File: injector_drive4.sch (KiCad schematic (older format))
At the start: 17 parts, among them P32 CONN_1, P33 CONN_1, Q16 PIP-3104, Q17 HALL

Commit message: Removed LM1815 options. Now adaptive mode and square waves are the default,
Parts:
- C52: Field1 (none) -> newark,97M4148; Field2 (none) -> vendor1, smd w hem; Field3 (none) -> vendor2, thru w hem; Field4 (none) -> vendor2, smd w hem; Field5 (none) -> 200,V; Field6 (none) -> 10,%; Field7 (none) -> Multilayer Ceramic; Field8 (none) -> other,more,stuff
- D88, D91: Field1 (none) -> vendor1, thru w hem; Field2 (none) -> vendor1, smd w hem; Field3 (none) -> vendor2, thru w hem; Field4 (none) -> vendor2, smd w hem; Field5 (none) -> reverse,V; Field6 (none) -> current,A; Field7 (none) -> x; Field8 (none) -> other,more,stuff
- D89: Field1 (none) -> newark,18M3533; Field2 (none) -> vendor1, smd w hem; Field3 (none) -> vendor2, thru w hem; Field4 (none) -> vendor2, smd w hem; Field5 (none) -> 500,mW; Field6 (none) -> 20,mA; Field7 (none) -> X; Field8 (none) -> other,more,stuff
- D90: Field1 (none) -> newark,58K2469; Field2 (none) -> vendor1, smd w hem; Field3 (none) -> vendor2, thru w hem; Field4 (none) -> vendor2, smd w hem; Field5 (none) -> x,x; Field6 (none) -> x,x; Field7 (none) -> construct; Field8 (none) -> other,more,stuff
- L4: Field1 (none) -> vendor1, thru w hem; Field2 (none) -> vendor1, smd w hem; Field3 (none) -> vendor2, thru w hem; Field4 (none) -> vendor2, smd w hem; Field5 (none) -> x,x; Field6 (none) -> x,x; Field7 (none) -> x; Field8 (none) -> other,more,stuff
- Q16: Field1 (none) -> digi,PIP3104-ND; Field2 (none) -> vendor1, smd w hem; Field3 (none) -> vendor2, thru w hem; Field4 (none) -> vendor2, smd w hem; Field5 (none) -> 8,A; Field6 (none) -> x,x; Field7 (none) -> TOPFET; Field8 (none) -> other,more,stuff
- Q17: Field1 (none) -> digi,480-2002-ND; Field2 (none) -> vendor1, smd w hem; Field3 (none) -> vendor2, thru w hem; Field4 (none) -> vendor2, smd w hem; Field5 (none) -> x,x; Field6 (none) -> x,x; Field7 (none) -> x; Field8 (none) -> other,more,stuff
- R122: Field1 (none) -> newark,38k0327; Field2 (none) -> vendor1, smd w hem; Field3 (none) -> vendor2, thru w hem; Field4 (none) -> vendor2, smd w hem; Field5 (none) -> 250,mW; Field6 (none) -> 5,%; Field7 (none) -> carbon film; Field8 (none) -> other,more,stuff
- R123: Field1 (none) -> newark,38K0329; Field2 (none) -> vendor1, smd w hem; Field3 (none) -> vendor2, thru w hem; Field4 (none) -> vendor2, smd w hem; Field5 (none) -> 250,mW; Field6 (none) -> 5,%; Field7 (none) -> carbon film; Field8 (none) -> other,more,stuff
- R124: Field1 (none) -> newark,38k0352; Field2 (none) -> vendor1, smd w hem; Field3 (none) -> vendor2, thru w hem; Field4 (none) -> vendor2, smd w hem; Field5 (none) -> 250,mW; Field6 (none) -> 5,%; Field7 (none) -> carbon film; Field8 (none) -> other,more,stuff
- R125: Field1 (none) -> vendor1, thru w hem; Field2 (none) -> vendor1, smd w hem; Field3 (none) -> vendor2, thru w hem; Field4 (none) -> vendor2, smd w hem; Field5 (none) -> power,W; Field6 (none) -> tol,%; Field7 (none) -> construct; Field8 (none) -> other,more,stuff
- R126: Field1 (none) -> newark,38K0352; Field2 (none) -> vendor1, smd w hem; Field3 (none) -> vendor2, thru w hem; Field4 (none) -> vendor2, smd w hem; Field5 (none) -> 250,mW; Field6 (none) -> 5,%; Field7 (none) -> carbon film; Field8 (none) -> other,more,stuff
- R127: Field1 (none) -> newark,59K8561; Field2 (none) -> vendor1, smd w hem; Field3 (none) -> vendor2, thru w hem; Field4 (none) -> vendor2, smd w hem; Field5 (none) -> 1,W; Field6 (none) -> 5,%; Field7 (none) -> construct; Field8 (none) -> other,more,stuff
- R128: Field1 (none) -> newark,38K0340; Field2 (none) -> vendor1, smd w hem; Field3 (none) -> vendor2, thru w hem; Field4 (none) -> vendor2, smd w hem; Field5 (none) -> 1/4,W; Field6 (none) -> 5,%; Field7 (none) -> carbon film; Field8 (none) -> other,more,stuff

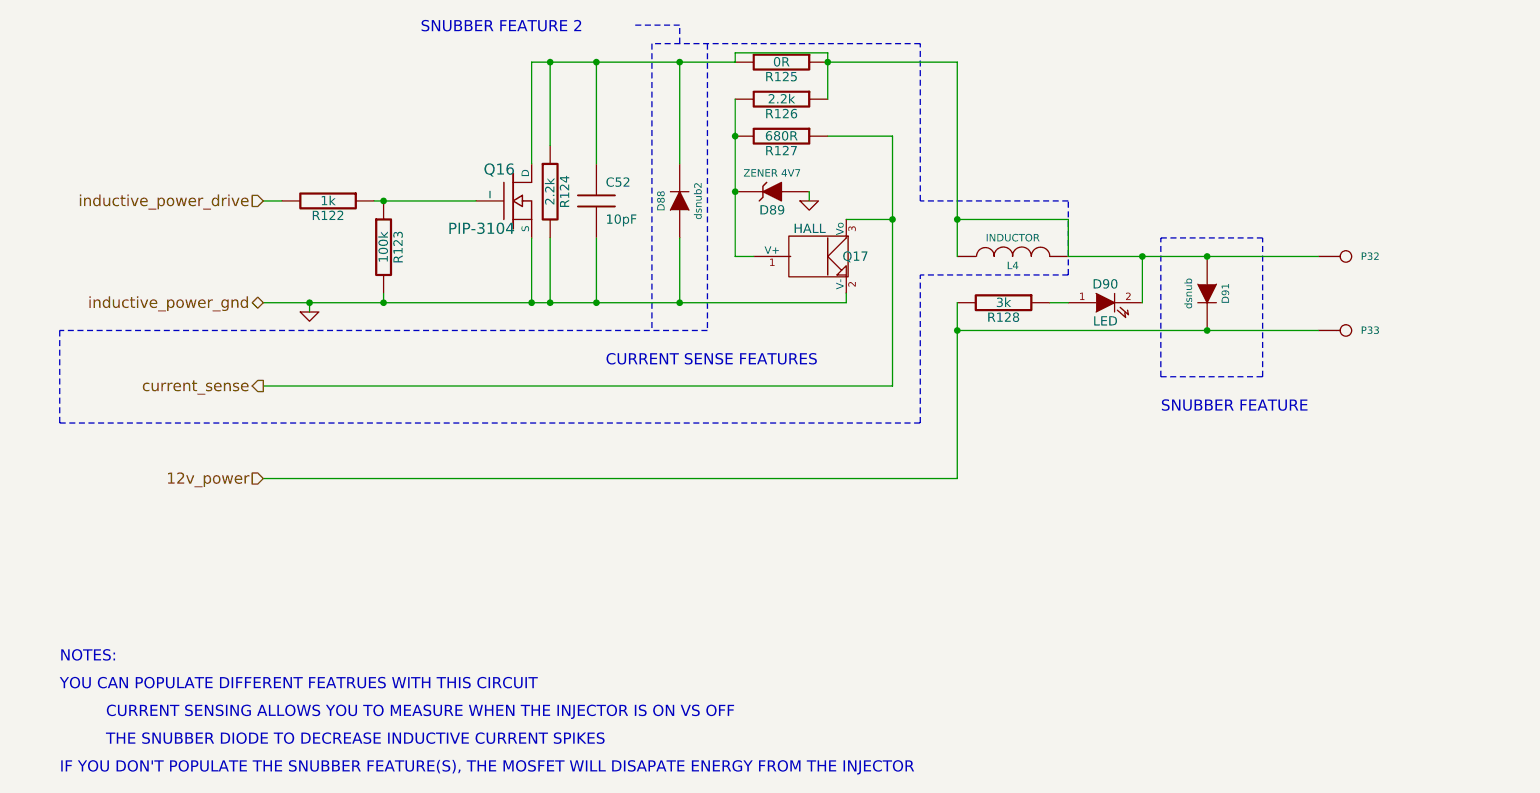
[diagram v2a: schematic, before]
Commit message: Implemented P&H, removed current sense circuitry, removed all unnecessary files from the repo
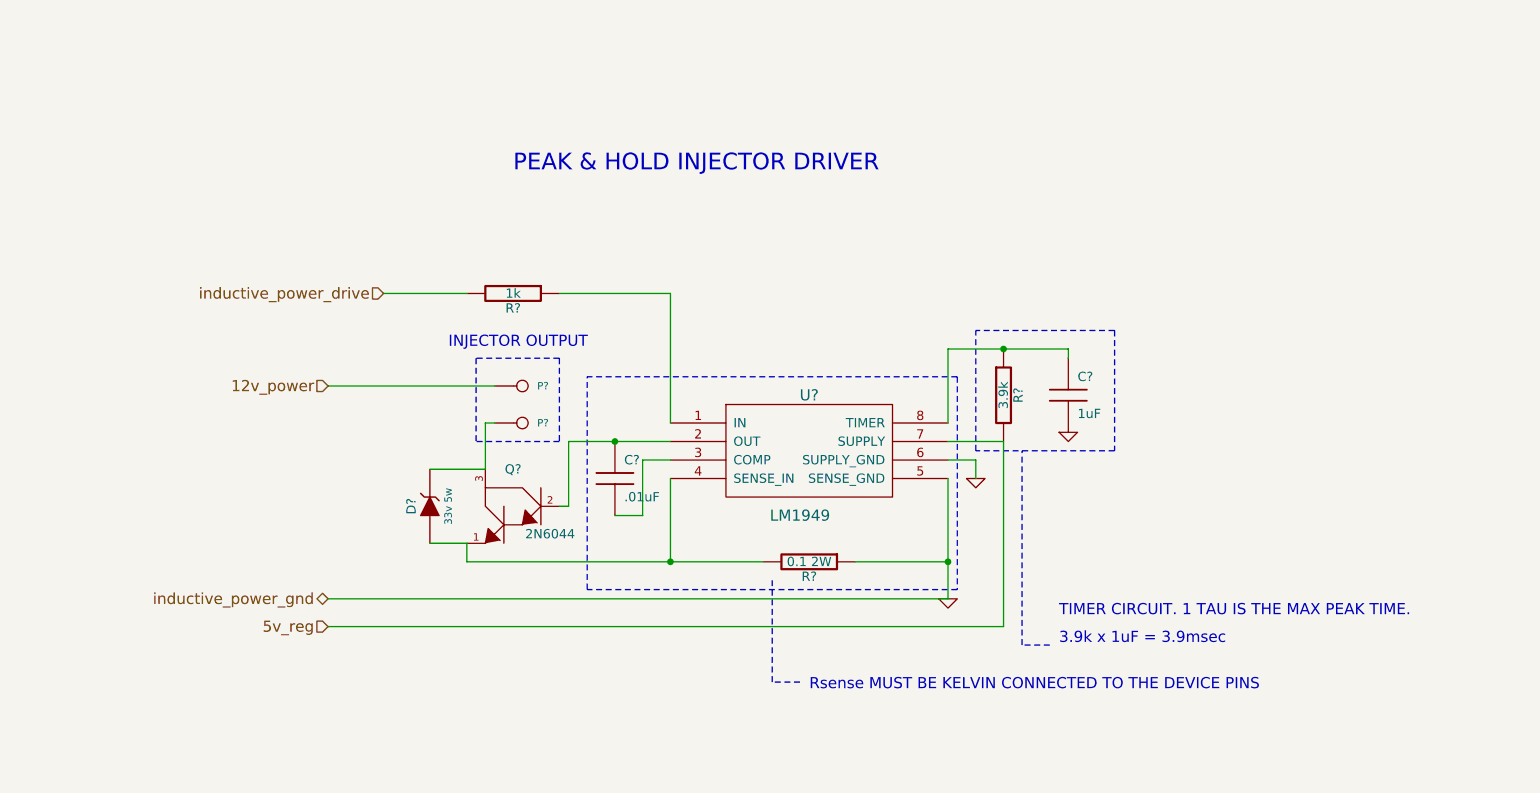
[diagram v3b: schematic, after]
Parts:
- removed C52: 10pF, C1V7, symbol C
- removed D88: dsnub2, D4-SMB, symbol DIODE
- removed D89: ZENER 4V7, D4-SMB, symbol ZENER
- removed D90: LED, LEDV, symbol LED
- removed D91: dsnub, D4-SMB, symbol DIODE
- removed L4: INDUCTOR, SIL-2, symbol INDUCTOR
- removed Q16: PIP-3104, TO220_sm, symbol PIP-3104
- removed Q17: HALL, SIL-3, symbol HALL
- removed R123: 100k, R4-SM0805, symbol R
- removed R124, R126: 2.2k, R4-SM0805, symbol R
- removed R125: 0R, R4-SM0805, symbol R
- removed R127: 680R, R4-SM0805, symbol R
- removed R128: 3k, R4-SM0805, symbol R
- added C?: .01uF, symbol C
- added C?: 1uF, symbol C
- added D?: 33v 5w, symbol ZENER
- added Q?: 2N6044, symbol DARL_N
- added R?: 0.1 2W, symbol R
- added R?: 3.9k, symbol R
- added U?: LM1949, DIP8, symbol LM1949
- renumbered P32 to P?, P33 to P?, R122 to R?
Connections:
- net 12v_power: now also P?.1; no longer P?.1
- net GND: now also C?.2, R?.1, U?.5 (SENSE_GND), U?.6 (SUPPLY_GND)
- net at R?.1: now also U?.1 (IN)
- new net: D?.2 (K), P?.1, Q?.3
- new net: C?.1, Q?.2, U?.2 (OUT)
- new net: C?.2, U?.3 (COMP)
- new net: D?.1 (A), Q?.1, R?.2, U?.4 (SENSE_IN)
- new net: C?.1, R?.1, U?.8 (TIMER)
- new net 5v_reg: R?.2, U?.7 (SUPPLY)
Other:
- note added: "3.9k x 1uF = 3.9msec"
- note added: "INJECTOR OUTPUT"
- note added: "PEAK & HOLD INJECTOR DRIVER"
- note added: "Rsense MUST BE KELVIN CONNECTED TO THE DEVICE PINS"
- note added: "TIMER CIRCUIT. 1 TAU IS THE MAX PEAK TIME."
- note removed: "CURRENT SENSE FEATURES"
- note removed: "CURRENT SENSING ALLOWS YOU TO MEASURE WHEN THE INJECTOR IS ON VS OFF"
- note removed: "IF YOU DON'T POPULATE THE SNUBBER FEATURE(S), THE MOSFET WILL DISAPATE ENERGY FROM THE INJECTOR"
- note removed: "NOTES:"
- note removed: "SNUBBER FEATURE"
- note removed: "SNUBBER FEATURE 2"
- note removed: "THE SNUBBER DIODE TO DECREASE INDUCTIVE CURRENT SPIKES"
- note removed: "YOU CAN POPULATE DIFFERENT FEATRUES WITH THIS CIRCUIT"
- moved on the sheet: P?, R?
